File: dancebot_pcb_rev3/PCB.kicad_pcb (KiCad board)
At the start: 2 copper layers, 63.5 x 53.3 mm, 30 parts, among them J1 Voltage Regulator, J10 NeoPixel Right Eye, J11 Rocker Switch, J2 IO14 servo 1, J3 IO13 servo 2, J4 IO12 servo 3, J5 IO15 servo 4, J6 IO18 servo 5 (hat), J8 Pins, J9 NeoPixel Left Eye, Q1 IRLML6402TRPBF, U1 IRLML2502TRPBF, U2 ESP32-DEVKITC-32U

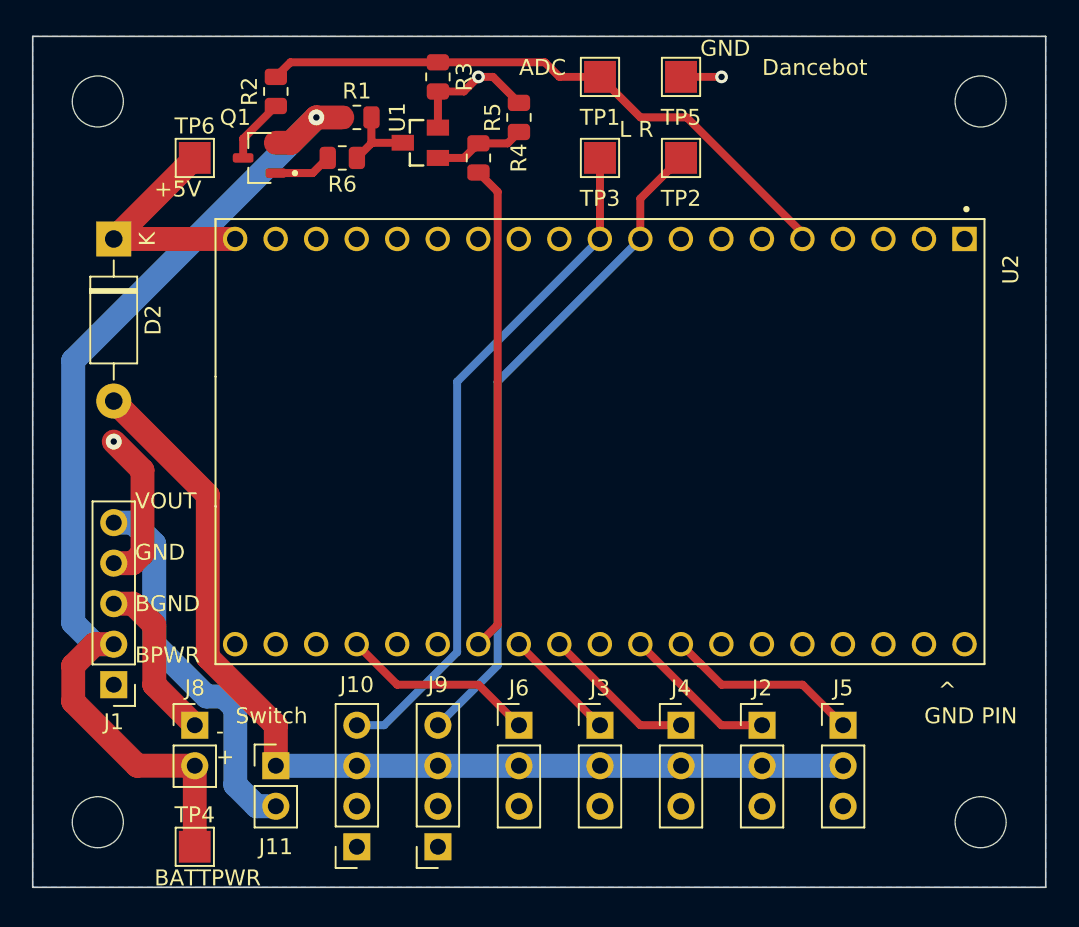
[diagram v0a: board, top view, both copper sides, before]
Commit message: changed BATT GND to GND, added some silkscreen labels
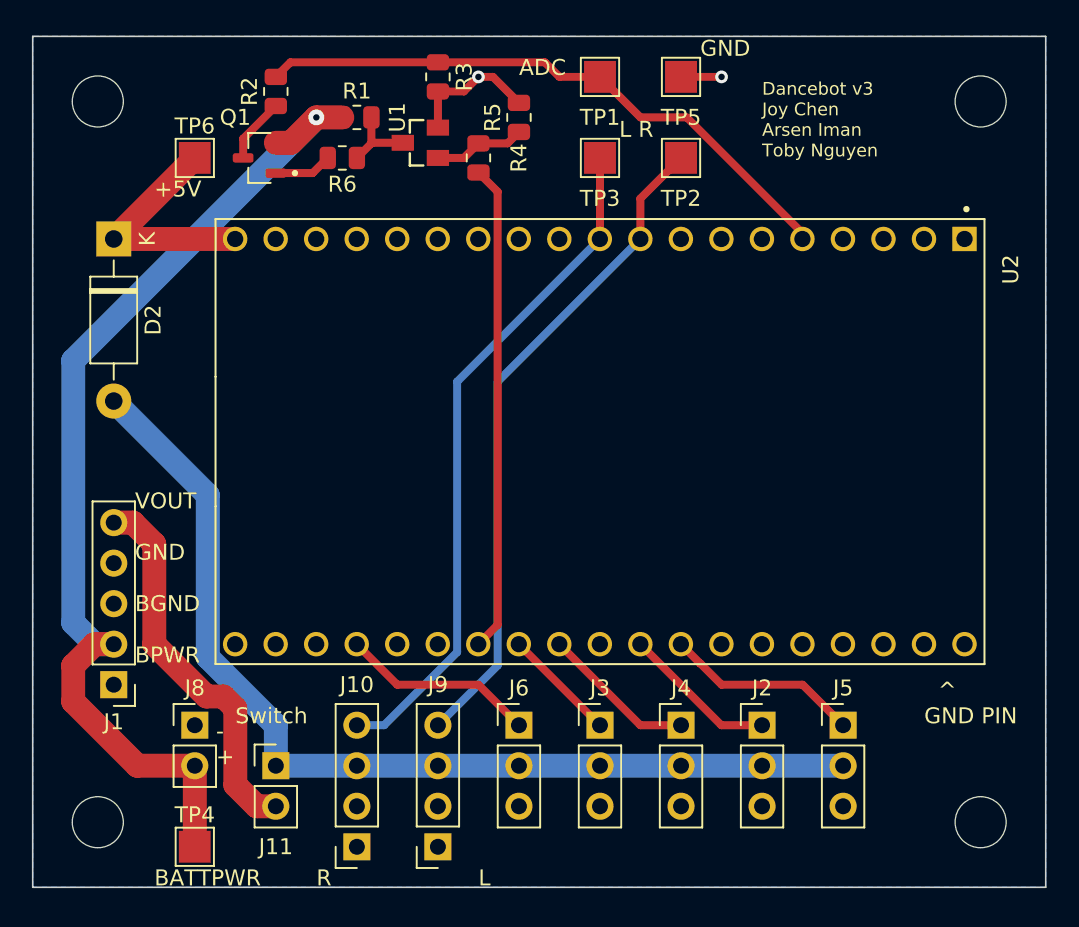
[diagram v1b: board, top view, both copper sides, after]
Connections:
- J1 pad 3: BATT GND -> GND
- J8 pad 1: BATT GND -> GND
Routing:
- net BATT GND: track 10.4 -> 0.00 mm
- net GND: track 20.8 -> 10.9 mm, vias 3 -> 2
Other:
- board text added: "Dancebot v3 Joy Chen Arsen Iman Toby Nguyen"
- board text added: "L"
- board text added: "R"
- board text removed: "Dancebot"

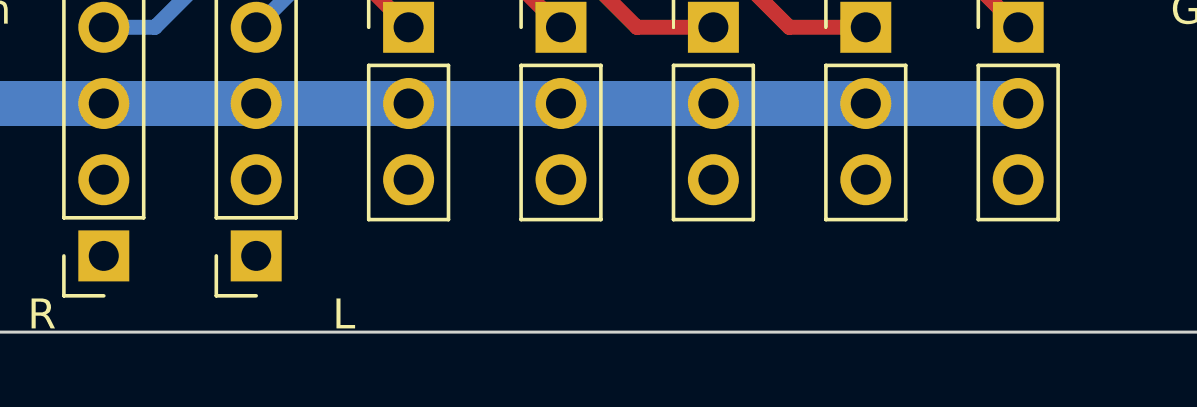
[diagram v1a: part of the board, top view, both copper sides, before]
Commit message: added silkscreen labels for servos
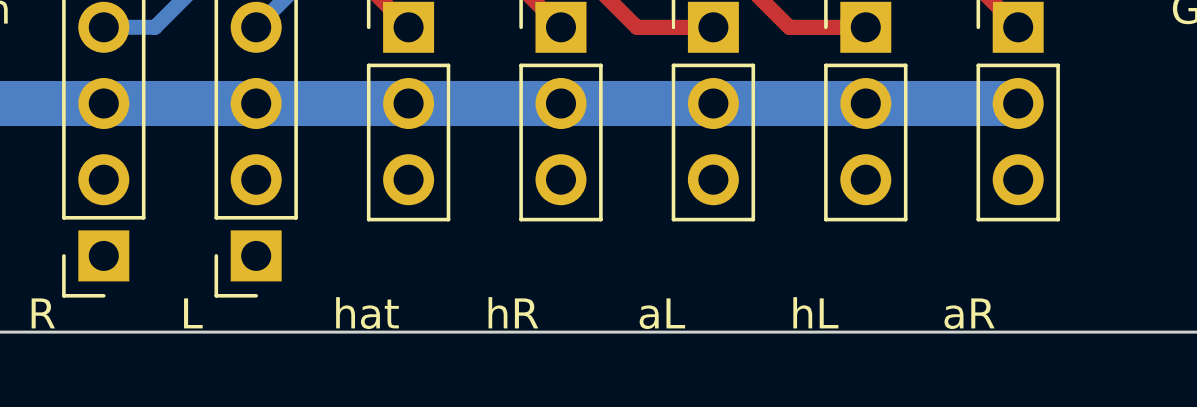
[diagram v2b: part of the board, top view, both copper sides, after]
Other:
- board text added: "aL"
- board text added: "aR"
- board text added: "hL"
- board text added: "hR"
- board text added: "hat"
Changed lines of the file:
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@@
     (effects (font (size 1 1) (thickness 0.15)) (justify left bottom))
   )
-  (gr_text "L" (at 226.06 127) (layer "F.SilkS")
+  (gr_text "L" (at 220.98 127) (layer "F.SilkS")
     (effects (font (size 1 1) (thickness 0.15)) (justify left bottom))
   )
@@
     (effects (font (size 1 1) (thickness 0.15)) (justify left bottom))
   )
+  (gr_text "hat" (at 226.06 127) (layer "F.SilkS")
+    (effects (font (size 1 1) (thickness 0.15)) (justify left bottom))
+  )
+  (gr_text "aL" (at 236.22 127) (layer "F.SilkS")
+    (effects (font (size 1 1) (thickness 0.15)) (justify left bottom))
+  )
   (gr_text "Dancebot v3\nJoy Chen\nArsen Iman\nToby Nguyen" (at 243.84 81.28) (layer "F.SilkS")
     (effects (font (size 0.8 0.8) (thickness 0.15)) (justify left bottom))
+  )
+  (gr_text "hL" (at 241.3 127) (layer "F.SilkS")
+    (effects (font (size 1 1) (thickness 0.15)) (justify left bottom))
   )
   (gr_text "L R" (at 234.88 80.08) (layer "F.SilkS")
@@
     (effects (font (size 1 1) (thickness 0.15)) (justify left bottom))
   )
+  (gr_text "aR" (at 246.38 127) (layer "F.SilkS")
+    (effects (font (size 1 1) (thickness 0.15)) (justify left bottom))
+  )
+  (gr_text "hR" (at 231.14 127) (layer "F.SilkS")
+    (effects (font (size 1 1) (thickness 0.15)) (justify left bottom))
+  )
